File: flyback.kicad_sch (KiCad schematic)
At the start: 43 parts, among them Q1 BSC109N10NS3G, Q2 STN3N40K3, Q3 IGB50N65S, Q4 IGB50N65S, U1 LT3750EMSTR, U2 ZXGD3009E6, U3 NCS325, U5 IX4427MTR, U9 MCP4562T-503E

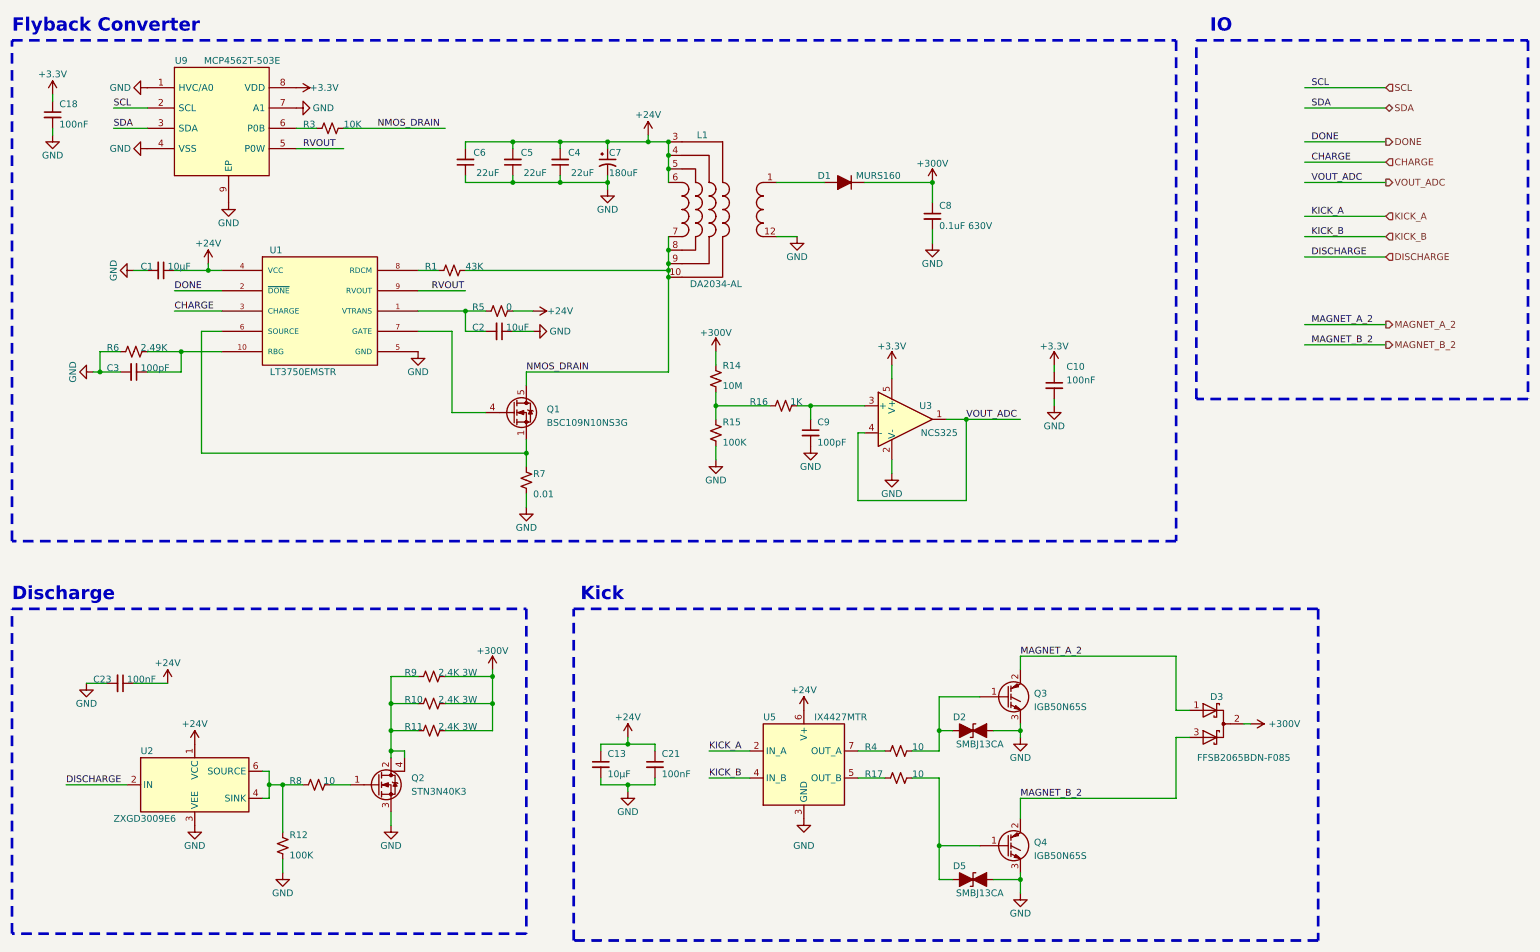
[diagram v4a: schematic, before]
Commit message: Move from stm32 to pic16 and remove other unnecessary parts.
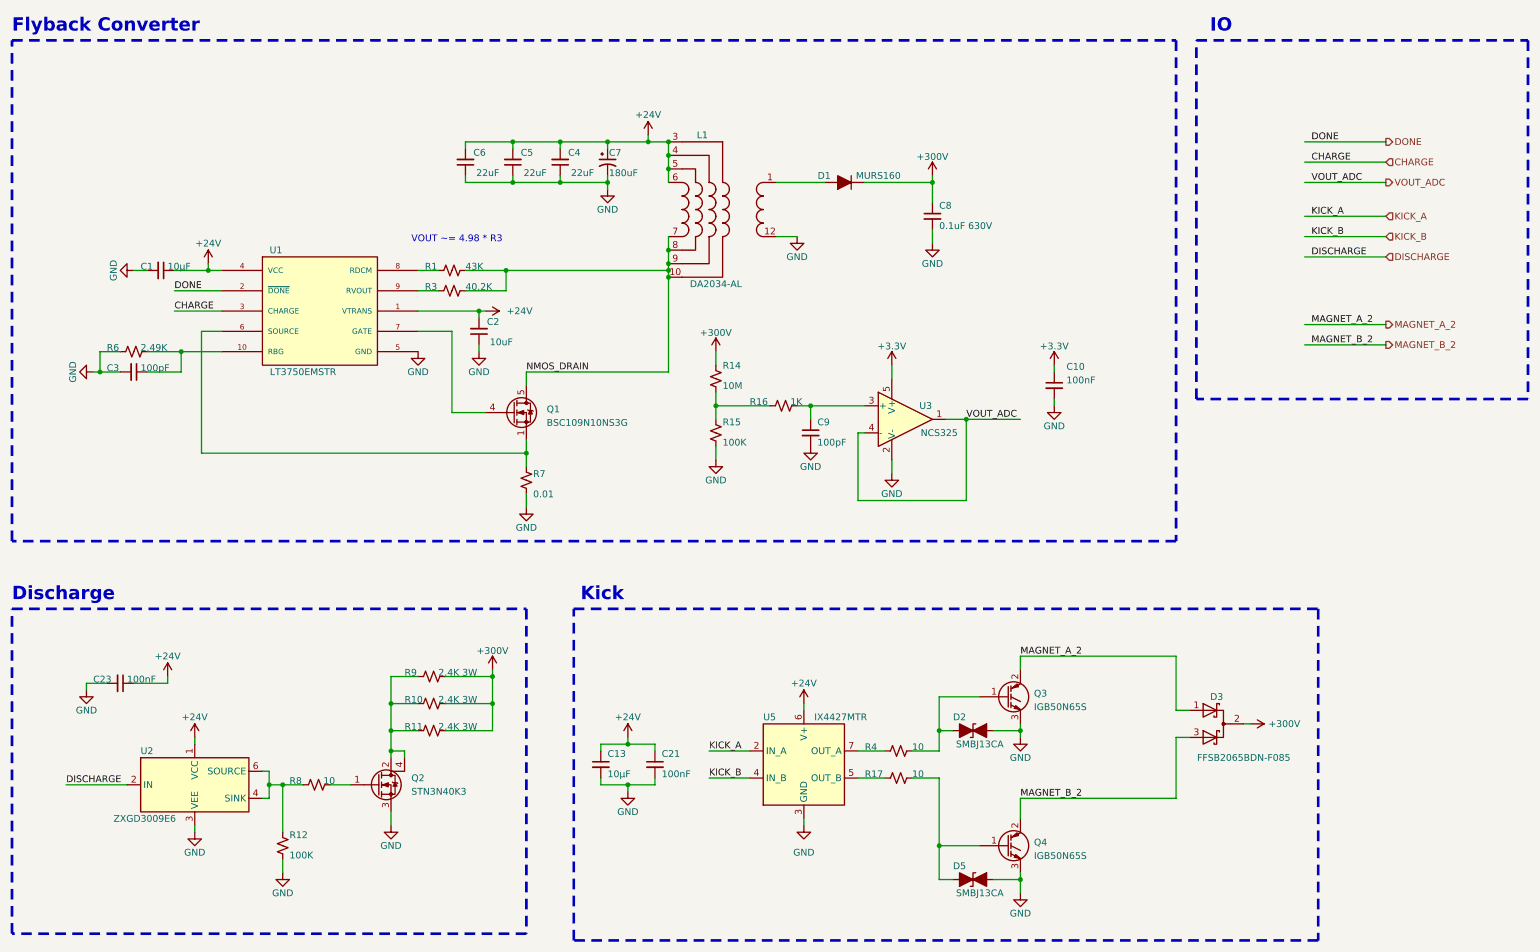
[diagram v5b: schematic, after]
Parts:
- removed C18: 100nF, Capacitor_SMD:C_0402_1005Metric_Pad0.74x0.62mm_HandSolder, symbol Device:C_Small
- removed R5: 0, Resistor_SMD:R_0402_1005Metric_Pad0.72x0.64mm_HandSolder, symbol Device:R_Small_US
- removed U9: MCP4562T-503E, MCP4562T-503E_MF:SON65P300X300X100-9N-D, symbol MCP4562T-503E_MF:MCP4562T-503E_MF
- C1, C13: footprint Capacitor_SMD:C_0805_2012Metric_Pad1.18x1.45mm_HandSolder -> Capacitor_SMD:C_0805_2012Metric
- C10, C23, C3, C9: footprint Capacitor_SMD:C_0402_1005Metric_Pad0.74x0.62mm_HandSolder -> Capacitor_SMD:C_0402_1005Metric
- C2: footprint Capacitor_SMD:C_1206_3216Metric_Pad1.33x1.80mm_HandSolder -> Capacitor_SMD:C_0603_1608Metric; JLCPCB Comment 10uF 25V X7R -> 10nF 35V X5R; JLCPCB Footprint 1206 -> 0603; MPN TMK316B7106KL-TD -> GRM188R6YA106MA73D
- C21: footprint Capacitor_SMD:C_0805_2012Metric_Pad1.18x1.45mm_HandSolder -> Capacitor_SMD:C_0402_1005Metric; JLCPCB Footprint 0805 -> 0402; MPN C0805C104M5RAC7800 -> GMC04X7R104K50NT
- C4, C5, C6: footprint Capacitor_SMD:C_1210_3225Metric_Pad1.33x2.70mm_HandSolder -> Capacitor_SMD:C_1210_3225Metric
- C8: footprint Capacitor_SMD:C_1812_4532Metric_Pad1.57x3.40mm_HandSolder -> Capacitor_SMD:C_1812_4532Metric
- D1, D2, D5: footprint Diode_SMD:D_SMB_Handsoldering -> Diode_SMD:D_SMB
- R1, R12, R17, R4, R6, R8: footprint Resistor_SMD:R_0402_1005Metric_Pad0.72x0.64mm_HandSolder -> Resistor_SMD:R_0402_1005Metric
- R10, R11, R9: footprint Resistor_SMD:R_2512_6332Metric_Pad1.40x3.35mm_HandSolder -> Resistor_SMD:R_2512_6332Metric
- R14, R16: footprint Resistor_SMD:R_0603_1608Metric_Pad0.98x0.95mm_HandSolder -> Resistor_SMD:R_0603_1608Metric
- R15: footprint Resistor_SMD:R_0603_1608Metric_Pad0.98x0.95mm_HandSolder -> Resistor_SMD:R_0402_1005Metric; JLCPCB Comment 100KΩ 0.1% -> 100KΩ 1%; JLCPCB Footprint 0603 -> 0402; MPN CRT0603-BY-1003ELF -> WR04X1003FTL
- R3: value 10K -> 40.2K; footprint Resistor_SMD:R_0402_1005Metric_Pad0.72x0.64mm_HandSolder -> Resistor_SMD:R_0402_1005Metric; JLCPCB Comment 10KΩ 1% -> 40.2KΩ 1%; MPN CR0402-FX-1002GLF -> RC0402FR-0740K2L
- R7: footprint Resistor_SMD:R_0805_2012Metric_Pad1.20x1.40mm_HandSolder -> Resistor_SMD:R_0805_2012Metric
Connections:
- net RVOUT is gone; now on an unnamed net: U1.9 (RVOUT)
- net +24V: now also C2.2, U1.1 (VTRANS)
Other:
- note added: "VOUT ~= 4.98 * R3"
- moved on the sheet: C2, R3

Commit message: Use the correct package for 4427.
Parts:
- U5: footprint Package_DFN_QFN:VDFN-8-1EP_2x2mm_P0.5mm_EP0.9x1.7mm -> Package_DFN_QFN:DFN-8-1EP_3x3mm_P0.65mm_EP1.7x2.05mm
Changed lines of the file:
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@@
       (effects (font (size 1.27 1.27)) (justify left))
     )
-    (property "Footprint" "Package_DFN_QFN:VDFN-8-1EP_2x2mm_P0.5mm_EP0.9x1.7mm" (at 158.75 175.26 0)
+    (property "Footprint" "Package_DFN_QFN:DFN-8-1EP_3x3mm_P0.65mm_EP1.7x2.05mm" (at 158.75 175.26 0)
       (effects (font (size 1.27 1.27)) hide)
     )

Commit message: Fix issues found during testing.
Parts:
- removed C23: 100nF, Capacitor_SMD:C_0402_1005Metric, symbol Device:C_Small
- removed R12: 100K, Resistor_SMD:R_0402_1005Metric, symbol Device:R_Small_US
- removed U2: ZXGD3009E6, Package_TO_SOT_SMD:SOT-23-6, symbol Driver_FET:ZXGD3009E6
- added C301: 10µF, Capacitor_SMD:C_0805_2012Metric, symbol Device:C_Small
- added C302: 100nF, Capacitor_SMD:C_0402_1005Metric, symbol Device:C_Small
- added RV301: 50K, Potentiometer_SMD:Potentiometer_Bourns_TC33X_Vertical, symbol Device:R_Potentiometer_Trim_US
- added U301: IX4427MTR, Package_DFN_QFN:DFN-8-1EP_3x3mm_P0.65mm_EP1.7x2.05mm, symbol Driver_FET:MIC4427
- R3: value 40.2K -> 10K; MPN RC0402FR-0740K2L -> RC1005F103CS
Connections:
- net +24V: now also C301.1, C302.1, U301.6 (V+)
- net DISCHARGE: now also U301.4 (IN_B)
- net GND: now also C301.2, C302.2, U301.3 (GND)
- net NMOS_DRAIN: now also RV301.2; no longer R3.1
- net at R8.2: now also U301.5 (OUT_B)
- new net: R3.1, RV301.1
- no-connect marks 0 -> 3
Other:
- moved on the sheet: R8

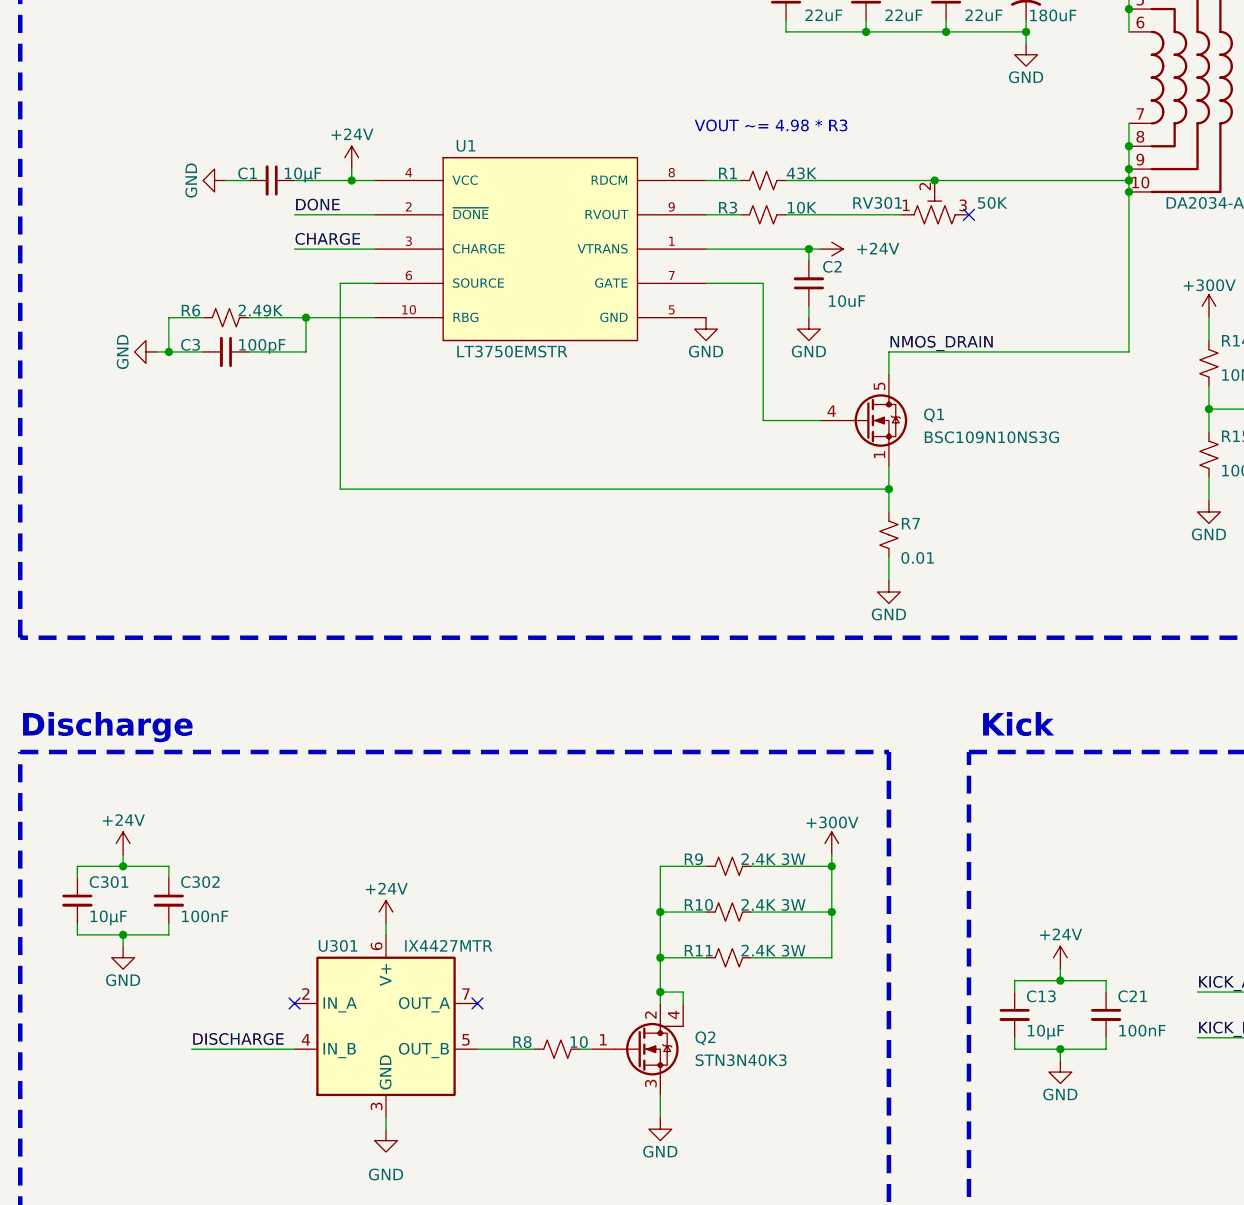
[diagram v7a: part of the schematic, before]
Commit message: Use parts similar to motor-driver where possible.
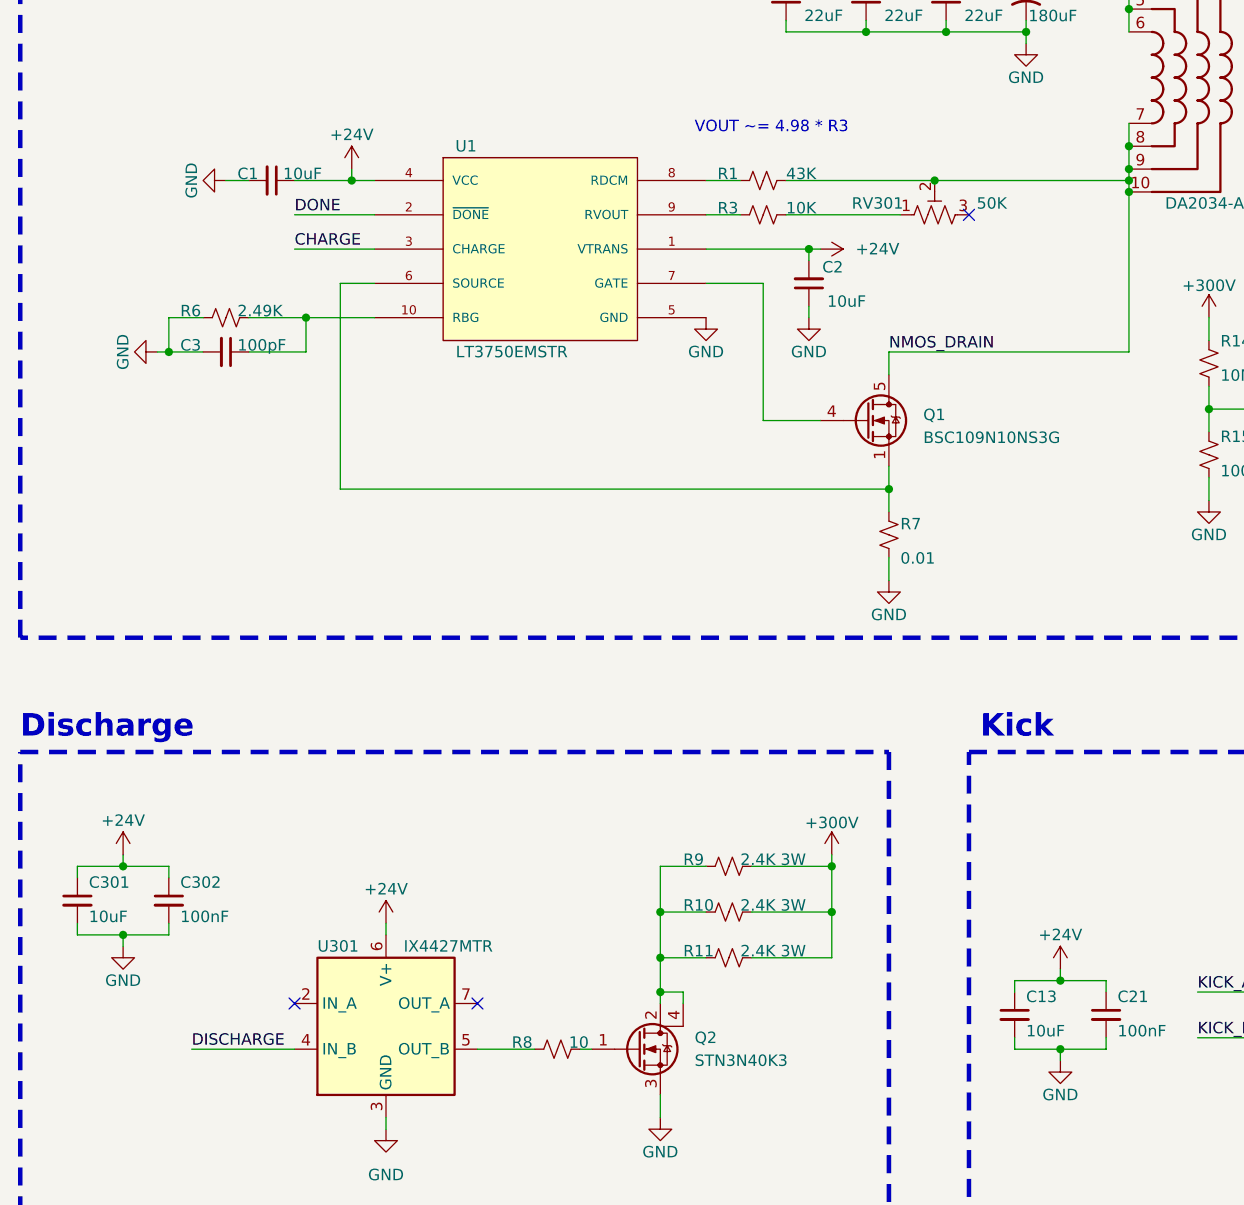
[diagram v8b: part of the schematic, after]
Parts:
- C1, C13, C301: value 10µF -> 10uF
- C10, C21, C302: MPN GMC04X7R104K50NT -> GRM155R71H104KE14J
- C3, C9: MPN 04025A101JAT2A -> 885012205055
- R17, R4, R8: MPN ERJ-2GEJ100X -> ERJ-2RKF10R0X
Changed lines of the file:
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@@
       (effects (font (size 1.27 1.27)) (justify left bottom))
     )
-    (property "Value" "10µF" (at 39.37 74.93 90)
+    (property "Value" "10uF" (at 39.37 74.93 90)
       (effects (font (size 1.27 1.27)) (justify left bottom))
     )
@@
       (effects (font (size 1.27 1.27)) hide)
     )
-    (property "MPN" "ERJ-2GEJ100X" (at 69.85 171.45 0)
+    (property "MPN" "ERJ-2RKF10R0X" (at 69.85 171.45 0)
       (effects (font (size 1.27 1.27)) hide)
     )
@@
       (effects (font (size 1.27 1.27)) hide)
     )
-    (property "MPN" "ERJ-2GEJ100X" (at 176.53 170.18 0)
+    (property "MPN" "ERJ-2RKF10R0X" (at 176.53 170.18 0)
       (effects (font (size 1.27 1.27)) hide)
     )
@@
       (effects (font (size 1.27 1.27)) (justify left bottom))
     )
-    (property "Value" "10µF" (at 17.78 157.48 0)
+    (property "Value" "10uF" (at 17.78 157.48 0)
       (effects (font (size 1.27 1.27)) (justify left bottom))
     )
@@
       (effects (font (size 1.27 1.27)) (justify left bottom))
     )
-    (property "Value" "10µF" (at 121.92 170.18 0)
+    (property "Value" "10uF" (at 121.92 170.18 0)
       (effects (font (size 1.27 1.27)) (justify left bottom))
     )
@@
       (effects (font (size 1.27 1.27)) hide)
     )
-    (property "MPN" "ERJ-2GEJ100X" (at 176.53 165.1 0)
+    (property "MPN" "ERJ-2RKF10R0X" (at 176.53 165.1 0)
       (effects (font (size 1.27 1.27)) hide)
     )
@@
       (effects (font (size 1.27 1.27)) hide)
     )
-    (property "MPN" "GMC04X7R104K50NT" (at 24.384 146.812 0)
+    (property "MPN" "GRM155R71H104KE14J" (at 24.384 146.812 0)
       (effects (font (size 1.27 1.27)) (justify left bottom) hide)
     )
@@
       (effects (font (size 1.27 1.27)) hide)
     )
-    (property "MPN" "GMC04X7R104K50NT" (at 128.524 159.512 0)
+    (property "MPN" "GRM155R71H104KE14J" (at 128.524 159.512 0)
       (effects (font (size 1.27 1.27)) (justify left bottom) hide)
     )
@@
       (effects (font (size 1.27 1.27)) hide)
     )
-    (property "MPN" "04025A101JAT2A" (at 160.02 105.41 0)
+    (property "MPN" "885012205055" (at 160.02 105.41 0)
       (effects (font (size 1.27 1.27)) hide)
     )
@@
       (effects (font (size 1.27 1.27)) hide)
     )
-    (property "MPN" "04025A101JAT2A" (at 33.02 93.98 0)
+    (property "MPN" "885012205055" (at 33.02 93.98 0)
       (effects (font (size 1.27 1.27)) hide)
     )
@@
       (effects (font (size 1.27 1.27)) hide)
     )
-    (property "MPN" "GMC04X7R104K50NT" (at 205.74 96.52 0)
-      (effects (font (size 1.27 1.27)) hide)
-    )
+    (property "MPN" "GRM155R71H104KE14J" (at 205.74 96.52 0)
+      (effects (font (size 1.27 1.27)) hide)
+    )
